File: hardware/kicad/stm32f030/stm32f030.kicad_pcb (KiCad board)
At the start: 2 copper layers, 108 parts, among them K1 RELAY_1RT, K2 RELAY_1RT, P1 CONN_01X02, P10 SWD, P2 LOOP, P3 LOOP, P4 RELAY OUT 1, P5 TTL OUT 1, P6 RELAY OUT 2, P7 TTL OUT 2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

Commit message: hardware/kicad/stm32f030: progress
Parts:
- added R28: 10k, Resistors_SMD:R_0603_HandSoldering, B.Cu at (69.2, 130.2)
- C16, C2, C3, C9, R25, R7, ZD1, ZD2: moved to B.Cu
- JP3: value JP3x1 -> boot0; footprint Pin_Headers:Pin_Header_Straight_1x03_Pitch2.54mm -> Pin_Headers:Pin_Header_Straight_1x02_Pitch2.54mm
- P1: value CONN_01X02 -> 5VIN
- P2: value LOOP -> LOOP1
- P3: value LOOP -> LOOP2
- moved C1 151.2 mm to (73.0, 151.1)
- moved U1 148.0 mm to (73.0, 144.8), turned to 270 degrees
- moved P1 144.9 mm to (73.0, 157.5)
- moved C3 140.8 mm to (74.3, 144.1)
- moved C2 135.3 mm to (73.0, 152.4)
- moved C9 116.7 mm to (55.4, 117.9), turned to 180 degrees
- moved C15 93.5 mm to (74.9, 127.6), turned to 180 degrees
- moved R26 93.4 mm to (78.5, 135.8), turned to 90 degrees
- moved C14 92.7 mm to (71.1, 127.6)
- moved C16 90.8 mm to (72.1, 136.9), turned to 270 degrees
- moved R25 89.8 mm to (73.8, 133.7), turned to 180 degrees
- moved SW3 89.3 mm to (70.9, 111.5)
- moved P8 88.2 mm to (66.7, 134.6)
- moved R27 88.2 mm to (80.1, 135.8), turned to 90 degrees
- moved R7 76.8 mm to (99.6, 146.8), turned to 270 degrees
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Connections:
- net Net-(P8-Pad1) renamed /MCU/TXD
- net Net-(P8-Pad2) renamed /MCU/RXD
- GDT2 pad 2: Earth -> Net-(GDT2-Pad2)
- GDT4 pad 2: Earth -> Net-(GDT4-Pad2)
- P10 pad 1: Net-(P10-Pad1) -> /MCU/SWC
- P10 pad 2: Net-(P10-Pad2) -> /MCU/SWD
- P2 pad 1: Net-(GDT1-Pad2) -> Net-(GDT1-Pad1)
- P2 pad 2: Earth -> Net-(GDT2-Pad2)
- P2 pad 3: Net-(GDT1-Pad1) -> Net-(GDT1-Pad2)
- P3 pad 1: Net-(GDT3-Pad2) -> Net-(GDT3-Pad1)
- P3 pad 2: Earth -> Net-(GDT4-Pad2)
- P3 pad 3: Net-(GDT3-Pad1) -> Net-(GDT3-Pad2)
- P9 pad 1: /MCU/scl -> /MCU/sda
- P9 pad 2: /MCU/sda -> /MCU/scl
- R14 pad 1: Net-(GDT3-Pad2) -> Net-(GDT3-Pad1)
- R14 pad 2: Earth -> Net-(GDT4-Pad2)
- R7 pad 1: Net-(GDT1-Pad2) -> Net-(GDT1-Pad1)
- R7 pad 2: Earth -> Net-(GDT2-Pad2)
- T1 pad 1: Net-(C5-Pad1) -> Net-(JP1-Pad2)
- T1 pad 3: Net-(JP1-Pad2) -> Net-(C5-Pad1)
- T2 pad 1: Net-(C10-Pad1) -> Net-(JP2-Pad2)
- T2 pad 3: Net-(JP2-Pad2) -> Net-(C10-Pad1)
- U2 pad 19: Net-(P10-Pad1) -> /MCU/SWD
- U2 pad 20: Net-(P10-Pad2) -> /MCU/SWC
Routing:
- net GND: track 14.7 -> 128.3 mm, vias 0 -> 3
- net Net-(C10-Pad1): track 5.02 -> 37.5 mm
- net +3V3: track 0.00 -> 30.0 mm, vias 0 -> 1
- net +5V: track 0.00 -> 28.1 mm, vias 0 -> 1
- net Net-(GDT1-Pad1): track 0.00 -> 26.8 mm
- net Net-(JP1-Pad2): track 0.00 -> 21.5 mm
- net Net-(C5-Pad1): track 0.00 -> 20.9 mm
- net Net-(GDT1-Pad2): track 0.00 -> 17.7 mm
- net Net-(C15-Pad1): track 0.00 -> 14.7 mm
- net Net-(GDT4-Pad2): track 0.00 -> 13.8 mm
- net Net-(GDT2-Pad2): track 0.00 -> 13.6 mm
- net /MCU/SWD: track 0.00 -> 12.9 mm
- net Net-(GDT3-Pad2): track 35.6 -> 22.7 mm
- net Net-(C14-Pad1): track 0.00 -> 12.5 mm
- net Earth: track 11.8 -> 0.00 mm
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
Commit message: hardware/kicad/stm32f030: progress
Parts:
- C4: moved to B.Cu
- U2: footprint Housings_SSOP:TSSOP-20_4.4x6.5mm_Pitch0.65mm -> Housings_SSOP:TSSOP-20_4.4x6.5mm_Pitch0.65mm_Handsoldering
- moved C17 68.0 mm to (96.6, 90.4)
- moved RN2 68.0 mm to (100.5, 81.0)
- moved RN3 68.0 mm to (84.2, 96.1)
- moved LED10 68.0 mm to (86.5, 89.7)
- moved LED13 68.0 mm to (86.5, 79.6)
- moved LED16 68.0 mm to (70.3, 89.7)
- moved LED18 68.0 mm to (70.3, 84.7)
- moved LED4 68.0 mm to (70.3, 79.6)
- moved LED5 68.0 mm to (86.5, 84.7)
- moved LED7 68.0 mm to (74.2, 99.8)
- moved RN4 68.0 mm to (80.0, 101.2)
- moved LED11 68.0 mm to (57.9, 101.8)
- moved LED12 68.0 mm to (94.6, 84.7)
- moved LED14 68.0 mm to (70.3, 94.8)
- moved LED15 68.0 mm to (66.1, 101.8)
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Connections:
- GDT2 pad 1: Net-(GDT1-Pad2) -> Net-(GDT2-Pad1)
- GDT2 pad 2: Net-(GDT2-Pad2) -> Net-(GDT1-Pad1)
- P2 pad 2: Net-(GDT2-Pad2) -> Net-(GDT1-Pad2)
- P2 pad 3: Net-(GDT1-Pad2) -> Net-(GDT2-Pad1)
- R7 pad 1: Net-(GDT1-Pad1) -> Net-(GDT2-Pad1)
- R7 pad 2: Net-(GDT2-Pad2) -> Net-(GDT1-Pad2)
- SW3 pad 1: Net-(SW3-Pad1) -> GND
- SW3 pad 2: Net-(SW3-Pad2) -> /MCU/reset
- T1 pad 1: Net-(JP1-Pad2) -> Net-(C5-Pad1)
- T1 pad 3: Net-(C5-Pad1) -> Net-(JP1-Pad2)
- T1 pad 4: Net-(GDT1-Pad2) -> Net-(GDT2-Pad1)
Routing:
- net GND: track 128.3 -> 202.0 mm, vias 3 -> 6
- net /colpitts/osc1: track 0.00 -> 39.7 mm, vias 0 -> 2
- net /MCU/osc1: track 0.00 -> 39.4 mm
- net +5V: track 28.1 -> 61.1 mm, vias 1 -> 2
- net Net-(GDT2-Pad1): track 0.00 -> 26.8 mm
- net Net-(C5-Pad1): track 20.9 -> 38.2 mm
- net /MCU/reset: track 3.65 -> 18.9 mm
- net Net-(GDT2-Pad2): track 13.6 -> 0.00 mm
- net Net-(GDT1-Pad1): track 26.8 -> 22.7 mm
- net +3V3: track 30.0 -> 34.0 mm, vias 1 -> 2
- net Net-(GDT1-Pad2): track 17.7 -> 13.8 mm
- net Net-(Q2-Pad1): track 0.00 -> 3.89 mm
- net Net-(C15-Pad1): track 14.7 -> 12.4 mm
- net Net-(JP2-Pad2): track 24.7 -> 22.5 mm
- net Net-(ZD3-Pad1): track 0.00 -> 2.19 mm
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
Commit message: hardware/kicad/stm32f030: modules ready
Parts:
- C14, C15, Q5, Q7, R26, R27: moved to B.Cu
- K1, K2: footprint Relays_THT:Relay_SANYOU_SRD_Series_Form_C -> relays:SRD-SL-C
- R28: moved to F.Cu
- RN1, RN2, RN3, RN4: footprint Resistors_SMD:R_Array_Convex_4x0603 -> Resistors_SMD:R_Array_Convex_4x0603_HandSoldering; moved to B.Cu
- moved P7 131.0 mm to (52.8, 122.2)
- moved Q8 123.0 mm to (58.4, 130.3)
- moved R24 119.1 mm to (56.9, 127.5)
- moved P5 113.4 mm to (69.3, 122.2)
- moved R22 111.5 mm to (61.5, 127.5), turned to 180 degrees
- moved R21 111.5 mm to (56.9, 124.0), turned to 180 degrees
- moved R20 111.2 mm to (61.5, 124.0), turned to 180 degrees
- moved R23 106.8 mm to (61.5, 125.7)
- moved LED1 106.0 mm to (73.4, 125.7)
- moved R19 104.7 mm to (73.4, 127.5)
- moved Q7 104.0 mm to (58.4, 130.3), turned to 180 degrees
- moved R17 99.5 mm to (78.0, 127.5), turned to 180 degrees
- moved R15 99.2 mm to (78.0, 124.0), turned to 180 degrees
- moved R16 98.4 mm to (73.4, 124.0), turned to 180 degrees
- moved D2 97.1 mm to (64.3, 131.8), turned to 270 degrees
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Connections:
- P8 pad 1: /MCU/TXD -> /MCU/RXD
- P8 pad 2: /MCU/RXD -> /MCU/TXD
- U3 pad 21: Net-(LED10-Pad1) -> Net-(LED3-Pad1)
- U3 pad 22: Net-(LED9-Pad1) -> Net-(LED4-Pad1)
- U3 pad 23: Net-(LED8-Pad1) -> Net-(LED5-Pad1)
- U3 pad 24: Net-(LED7-Pad1) -> Net-(LED6-Pad1)
- U3 pad 25: Net-(LED6-Pad1) -> Net-(LED7-Pad1)
- U3 pad 26: Net-(LED5-Pad1) -> Net-(LED8-Pad1)
- U3 pad 27: Net-(LED4-Pad1) -> Net-(LED9-Pad1)
- U3 pad 28: Net-(LED3-Pad1) -> Net-(LED10-Pad1)
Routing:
- net +5V: track 61.1 -> 149.0 mm, vias 2 -> 3
- net GND: track 202.0 -> 162.2 mm, vias 6 -> 7
- net /colpitts/osc1: track 39.7 -> 0.00 mm, vias 2 -> 0
- net /MCU/osc1: track 39.4 -> 0.00 mm
- net Net-(LED3-Pad1): track 0.00 -> 26.8 mm
- net Net-(LED4-Pad1): track 0.00 -> 25.5 mm
- net Net-(LED10-Pad1): track 0.00 -> 24.8 mm
- net Net-(LED9-Pad1): track 0.00 -> 24.5 mm
- net Net-(LED8-Pad1): track 0.00 -> 24.4 mm
- net Net-(LED7-Pad1): track 0.00 -> 24.2 mm
- net Net-(LED5-Pad1): track 0.00 -> 24.1 mm
- net Net-(LED6-Pad1): track 0.00 -> 23.9 mm
- net Net-(K2-Pad5): track 0.00 -> 22.2 mm
- net Net-(K1-Pad5): track 0.00 -> 22.0 mm
- net Net-(R22-Pad2): track 0.00 -> 15.8 mm
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
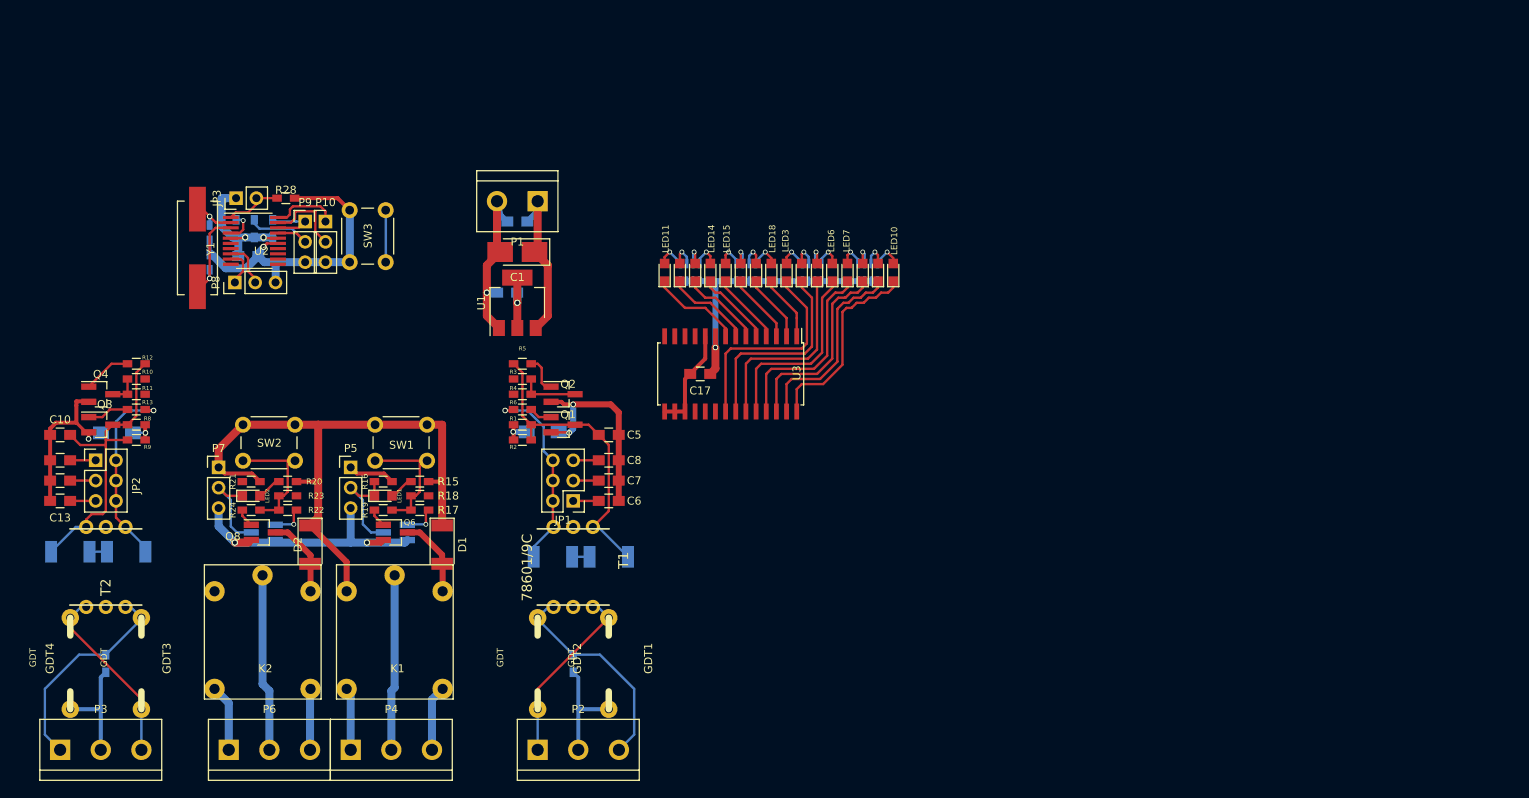
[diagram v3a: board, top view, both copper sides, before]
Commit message: slight;y modified module layout
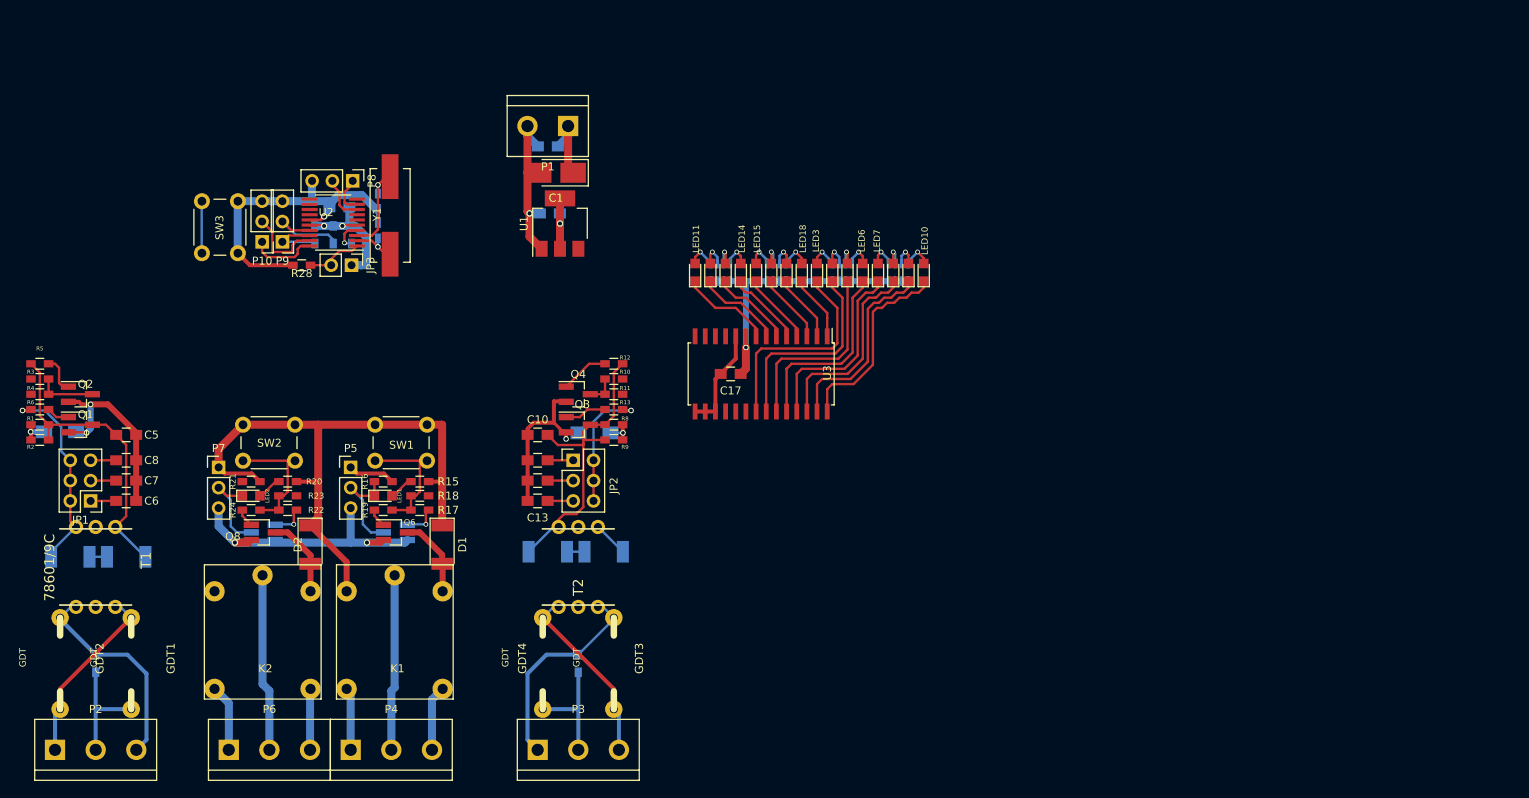
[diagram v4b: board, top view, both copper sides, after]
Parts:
- moved JP1 60.3 mm to (36.8, 126.4)
- moved P2 60.3 mm to (37.5, 157.5)
- moved Q1 60.3 mm to (35.6, 116.8)
- moved Q2 60.3 mm to (35.6, 113.0)
- moved R1 60.3 mm to (30.5, 116.8)
- moved R2 60.3 mm to (30.5, 118.7)
- moved R3 60.3 mm to (30.5, 111.1)
- moved R4 60.3 mm to (30.5, 113.0)
- moved R5 60.3 mm to (30.5, 109.2)
- moved R6 60.3 mm to (30.5, 114.9)
- moved C4 60.3 mm to (33.0, 117.7)
- moved C5 60.3 mm to (41.3, 118.1)
- moved C6 60.3 mm to (41.3, 126.4)
- moved C7 60.3 mm to (41.3, 123.8)
- moved C8 60.3 mm to (41.3, 121.3)
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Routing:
- net +5V: track 149.0 -> 137.7 mm
- net Net-(JP2-Pad2): track 24.2 -> 20.7 mm
- net GND: track 162.2 -> 161.3 mm
- net Net-(C5-Pad1): track 38.2 -> 37.3 mm
- net Net-(JP1-Pad2): track 24.6 -> 25.2 mm

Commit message: more optimizations on modules
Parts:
- moved SW3 21.9 mm to (45.0, 69.6)
- moved P10 21.7 mm to (48.3, 74.7)
- moved P9 21.7 mm to (50.8, 74.7)
- moved R28 20.6 mm to (53.1, 79.0)
- moved U1 20.6 mm to (98.7, 71.4), turned to 180 degrees
- moved R5 19.7 mm to (49.1, 115.4)
- moved C14 19.7 mm to (62.5, 72.1)
- moved C16 19.7 mm to (57.6, 72.9)
- moved C15 19.7 mm to (62.5, 75.8)
- moved P8 19.7 mm to (59.3, 69.6)
- moved Y1 19.7 mm to (64.0, 73.9)
- moved JP3 19.7 mm to (59.2, 80.1)
- moved R25 19.7 mm to (59.2, 76.3)
- moved R26 19.7 mm to (56.9, 76.3)
- moved U2 19.7 mm to (56.9, 74.8)
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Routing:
- net /MCU/reset: track 10.3 -> 30.2 mm
- net Net-(C5-Pad1): track 37.3 -> 20.3 mm
- net GND: track 161.3 -> 178.2 mm
- net +5V: track 137.7 -> 154.5 mm
- net /MCU/scl: track 11.6 -> 16.5 mm
- net Net-(Q2-Pad1): track 4.78 -> 9.58 mm
- net Net-(JP1-Pad2): track 25.2 -> 23.3 mm, vias 1 -> 0
- net /MCU/sda: track 7.88 -> 9.19 mm
- net /MCU/SWC: track 8.42 -> 7.52 mm
- net /MCU/SWD: track 10.0 -> 9.27 mm
- net Net-(Q6-Pad1): track 3.03 -> 2.31 mm

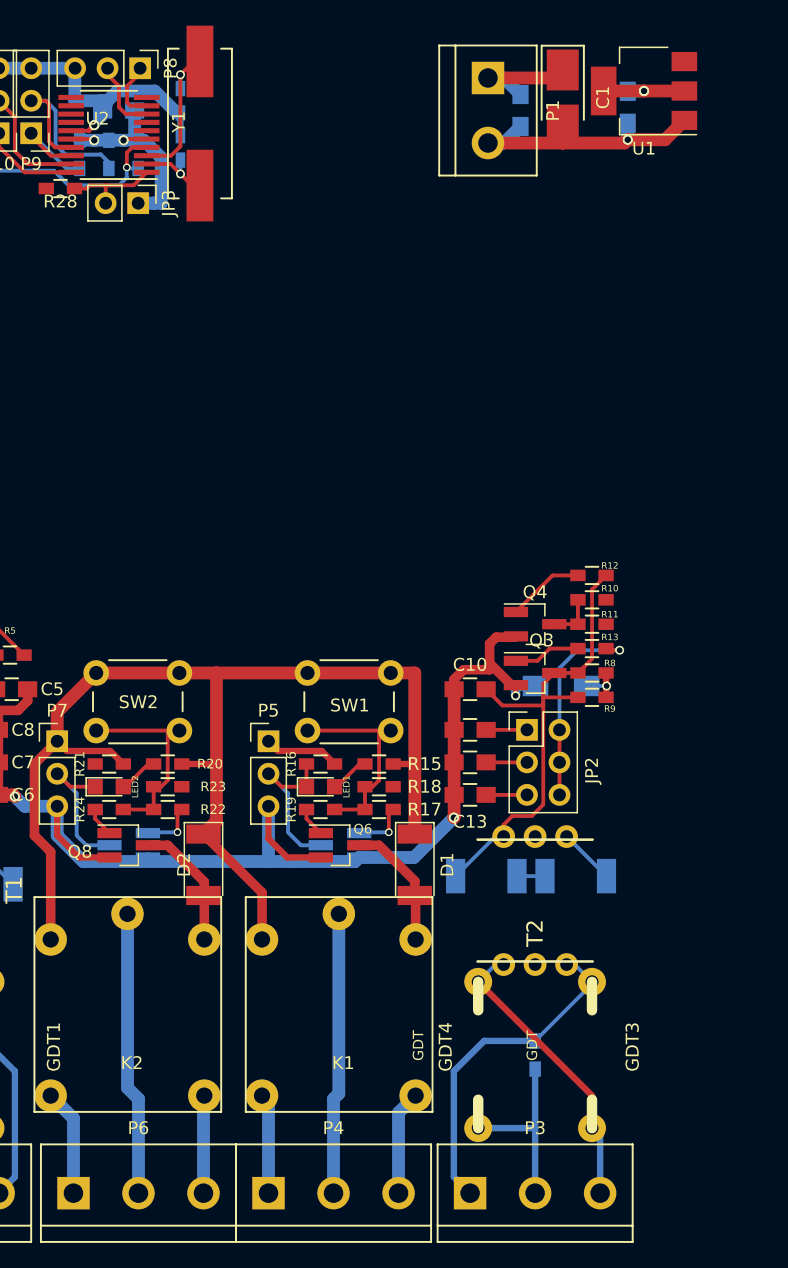
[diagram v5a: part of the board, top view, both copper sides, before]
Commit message: space for mounting hole
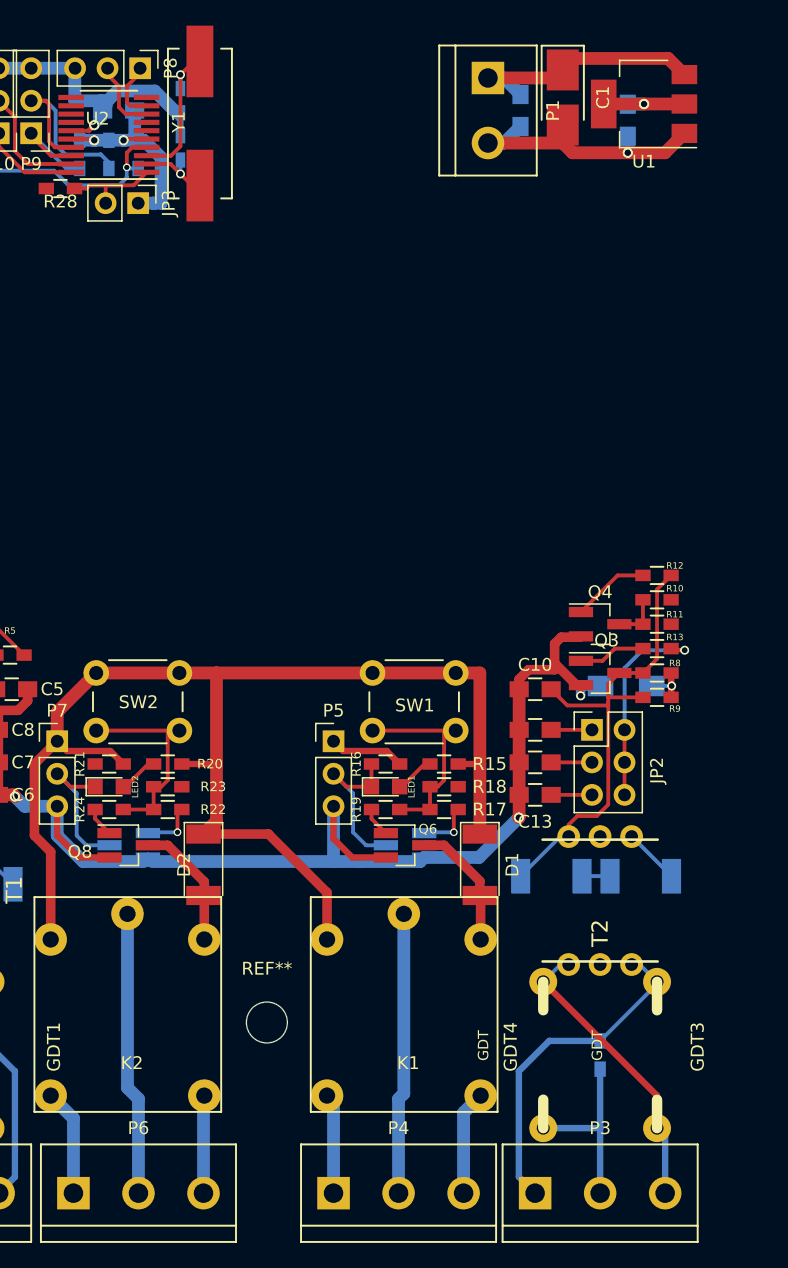
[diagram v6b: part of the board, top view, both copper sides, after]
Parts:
- added REF**: MountingHole_3.2mm_M3, Mounting_Holes:MountingHole_3.2mm_M3, F.Cu at (69.2, 144.1)
- moved GDT4 5.08 mm to (90.8, 146.7)
- moved R15 5.08 mm to (83.1, 124.0)
- moved R17 5.08 mm to (83.1, 127.5)
- moved R18 5.08 mm to (83.1, 125.7)
- moved C10 5.08 mm to (90.2, 118.1)
- moved C11 5.08 mm to (90.2, 121.3)
- moved C12 5.08 mm to (90.2, 123.8)
- moved C13 5.08 mm to (90.2, 126.4)
- moved C9 5.08 mm to (97.3, 117.9)
- moved D1 5.08 mm to (85.9, 131.8)
- moved GDT3 5.08 mm to (99.7, 146.7)
- moved JP2 5.08 mm to (94.6, 121.3)
- moved K1 5.08 mm to (73.9, 149.9)
- moved LED1 5.08 mm to (78.5, 125.7)
- moved P3 5.08 mm to (95.2, 157.5)
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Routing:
- net +5V: track 154.5 -> 175.0 mm
- net GND: track 178.2 -> 184.6 mm

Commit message: PCB V0.90
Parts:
- added REF**: MountingHole_3.2mm_M3, Mounting_Holes:MountingHole_3.2mm_M3, F.Cu at (40.6, 96.5)
- added REF**: MountingHole_3.2mm_M3, Mounting_Holes:MountingHole_3.2mm_M3, F.Cu at (99.1, 104.8)
- moved LED17 47.5 mm to (84.6, 96.4)
- moved LED18 47.5 mm to (86.5, 96.4)
- moved LED11 47.5 mm to (73.2, 96.4)
- moved LED12 47.5 mm to (75.1, 96.4)
- moved LED15 47.5 mm to (80.8, 96.4)
- moved LED16 47.5 mm to (82.7, 96.4)
- moved RN1 47.5 mm to (91.6, 96.4)
- moved RN2 47.5 mm to (98.6, 96.4)
- moved RN3 47.5 mm to (76.3, 96.4)
- moved RN4 47.5 mm to (83.3, 96.4)
- moved LED10 47.5 mm to (101.7, 96.4)
- moved LED13 47.5 mm to (77.0, 96.4)
- moved LED14 47.5 mm to (78.9, 96.4)
- moved LED3 47.5 mm to (88.4, 96.4)
- moved LED4 47.5 mm to (90.3, 96.4)
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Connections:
- P10 pad 1: /MCU/SWC -> /MCU/SWD
- P10 pad 2: /MCU/SWD -> /MCU/SWC
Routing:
- net +3V3: track 26.1 -> 110.6 mm, vias 3 -> 4
- net /colpitts/osc1: track 0.00 -> 73.3 mm, vias 0 -> 2
- net /outputs/active1: track 0.00 -> 61.0 mm, vias 0 -> 4
- net GND: track 184.6 -> 234.0 mm, vias 7 -> 10
- net +5V: track 175.0 -> 218.2 mm, vias 3 -> 4
- net /MCU/active1: track 0.00 -> 40.9 mm, vias 0 -> 2
- net /MCU/sda: track 9.19 -> 49.3 mm, vias 0 -> 2
- net /MCU/scl: track 16.5 -> 53.9 mm, vias 0 -> 2
- net /MCU/reset: track 30.2 -> 63.7 mm, vias 1 -> 4
- net /MCU/osc1: track 0.00 -> 21.6 mm
- net Net-(C5-Pad1): track 20.3 -> 30.6 mm
- net /MCU/SWC: track 7.52 -> 13.0 mm
- net Net-(R22-Pad2): track 15.8 -> 21.0 mm, vias 0 -> 1
- net Net-(JP2-Pad2): track 20.7 -> 23.8 mm
- net Net-(LED11-Pad1): track 11.5 -> 14.5 mm
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- added copper zone on B.Cu, net GND
- added copper zone on F.Cu, net GND
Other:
- board outline added: 67.3 x 68.6 mm
